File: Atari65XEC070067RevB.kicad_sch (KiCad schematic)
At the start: 340 parts, among them J1 SIO, J2 MONITOR, J5 JOY1, J6 JOY1, J7 DIN-7, J8 KEYBOARD, Q1 2N3904, Q2 2N3904, Q3 2N3904, Q4 2N3904, Q5 2N3904, Q6 2N3904, Q7 MPSA55, SW1 SW_SPDT, U1 LM358, U10 4164, U11 4164, U12 4164, U13 4164, U14 4164, U15 4164, U16 4164, U17 C014889/GTIA, U18 74LS08, U19 NE555P, U2 74LS138, U20 4050, U21 74LS74, U22 C012294/POKEY, U23 C014795 PIA/6520, U24 4051, U25 4051, U26 4164, U27 4164, U28 4164, U29 4164, U3 MMU, U30 4164, U31 4164, U32 4164, U33 4164, U34 MMMU, U35 74LS95, U4 BASIC, U5 OS ROM, U6 CO14806/SALLY, U7 C021698/ANTIC, U8 C061991/FREDDIE, U9 4164, Y2 4.33618MHz

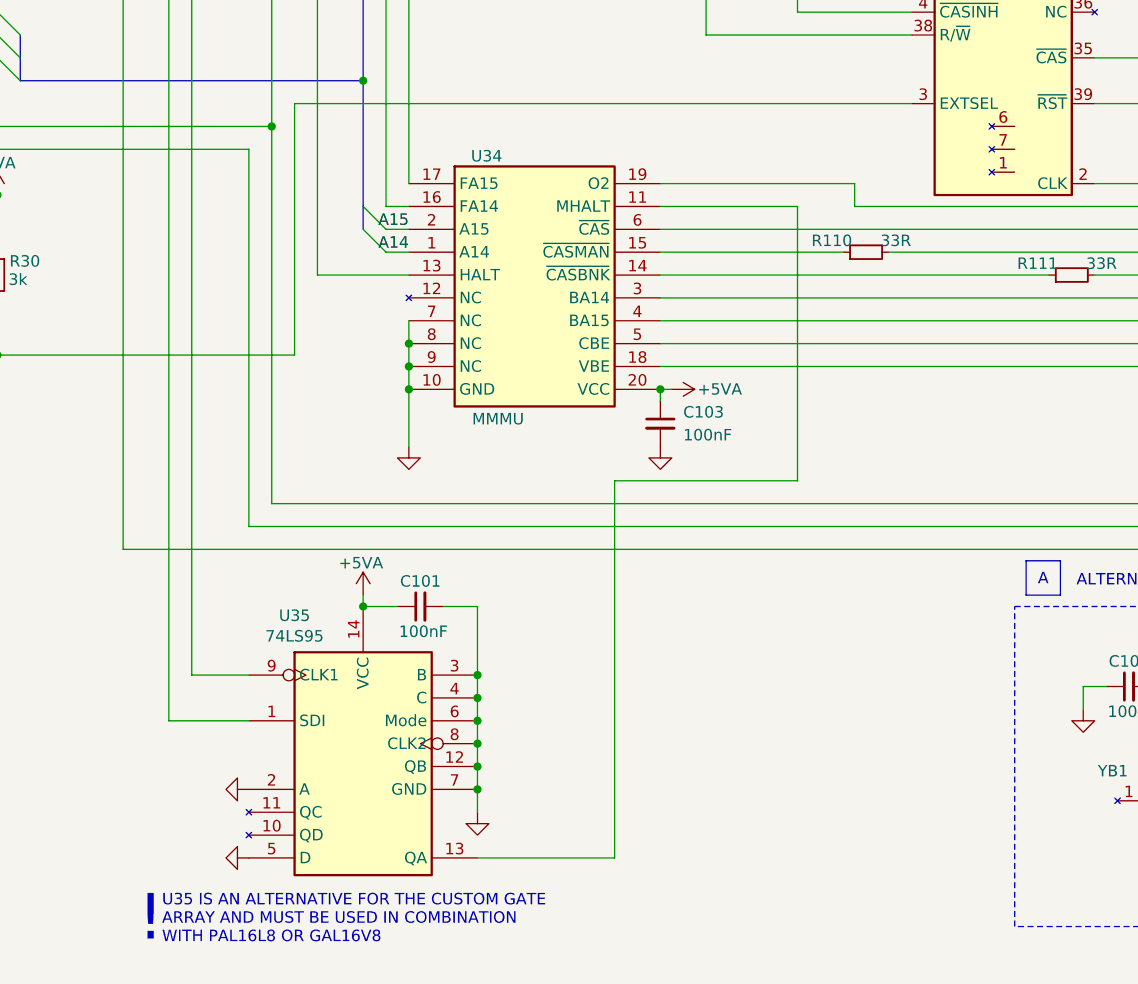
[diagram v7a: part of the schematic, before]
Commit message: update u35 and u34 schematic and routing
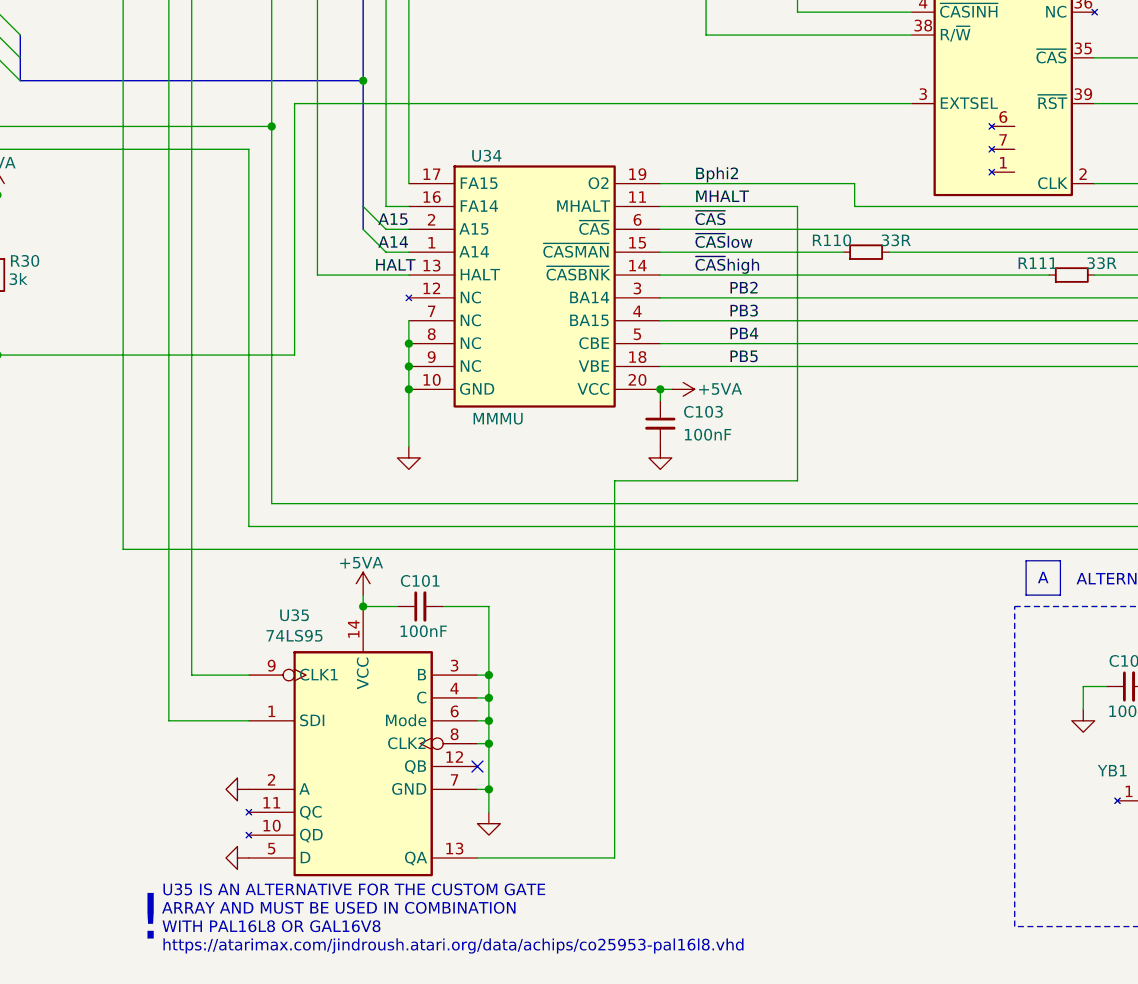
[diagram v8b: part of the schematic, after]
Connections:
- net GND: no longer U35.12 (QB)
- net PB4: now reaches R24.2, U23.14 (PB4), U34.5 (CBE)
- net MHALT: now reaches U34.11 (MHALT), U35.13 (QA)
- net ~{CAS}high: now reaches R111.1, U34.14 (~{CASBNK})
- net ~{CAS}low: now reaches R110.1, U34.15 (~{CASMAN})
- net PB5: now reaches R206.1, U23.15 (PB5), U34.18 (VBE)
- net Bphi2: now reaches R20.1, U18.1, U34.19 (O2), U6.39 (O2), U8.5 (O2)
- net PB2: now reaches R23.2, U23.12 (PB2), U34.3 (BA14)
- net PB3: now reaches R25.2, U23.13 (PB3), U34.4 (BA15)
- net ~{CAS}: now reaches U34.6 (~{CAS}), U8.35 (~{CAS})
- no-connect marks 13 -> 14
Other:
- note added: "U35 IS AN ALTERNATIVE FOR THE CUSTOM GATE ARRAY AND MUST BE USED IN COMBINATION WITH PAL16L8 OR GAL16V8 https://atarimax.com/jindroush.atari.org/data/achips/co25953-pal16l8.vhd"
- note removed: "U35 IS AN ALTERNATIVE FOR THE CUSTOM GATE ARRAY AND MUST BE USED IN COMBINATION WITH PAL16L8 OR GAL16V8"
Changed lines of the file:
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@@
 		)
 	)
-	(text "U35 IS AN ALTERNATIVE FOR THE CUSTOM GATE\nARRAY AND MUST BE USED IN COMBINATION\nWITH PAL16L8 OR GAL16V8"
+	(text "U35 IS AN ALTERNATIVE FOR THE CUSTOM GATE\nARRAY AND MUST BE USED IN COMBINATION\nWITH PAL16L8 OR GAL16V8\nhttps://atarimax.com/jindroush.atari.org/data/achips/co25953-pal16l8.vhd"
 		(exclude_from_sim no)
 		(at 55.118 400.558 0)
@@
 	)
 	(junction
-		(at 90.17 383.54)
-		(diameter 0)
-		(color 0 0 0 0)
-	)
-	(junction
 		(at 511.81 265.43)
 		(diameter 0)
@@
 	)
 	(junction
-		(at 90.17 386.08)
-		(diameter 0)
-		(color 0 0 0 0)
-	)
-	(junction
 		(at 490.22 153.67)
 		(diameter 0)
@@
 	)
 	(junction
+		(at 91.44 373.38)
+		(diameter 0)
+		(color 0 0 0 0)
+	)
+	(junction
 		(at 195.58 133.35)
 		(diameter 0)
@@
 	)
 	(junction
+		(at 91.44 378.46)
+		(diameter 0)
+		(color 0 0 0 0)
+	)
+	(junction
 		(at 384.81 336.55)
 		(diameter 0)
@@
 	)
 	(junction
+		(at 91.44 386.08)
+		(diameter 0)
+		(color 0 0 0 0)
+	)
+	(junction
 		(at 322.58 64.77)
 		(diameter 0)
@@
 	)
 	(junction
-		(at 90.17 378.46)
-		(diameter 0)
-		(color 0 0 0 0)
-	)
-	(junction
 		(at 515.62 257.81)
 		(diameter 0)
@@
 	)
 	(junction
-		(at 90.17 375.92)
-		(diameter 0)
-		(color 0 0 0 0)
-	)
-	(junction
 		(at 387.35 165.1)
 		(diameter 0)
@@
 	)
 	(junction
+		(at 91.44 375.92)
+		(diameter 0)
+		(color 0 0 0 0)
+	)
+	(junction
 		(at 278.13 317.5)
 		(diameter 0)
@@
 	)
 	(junction
+		(at 91.44 381)
+		(diameter 0)
+		(color 0 0 0 0)
+	)
+	(junction
 		(at 234.95 271.78)
 		(diameter 0)
@@
 	)
 	(junction
-		(at 90.17 381)
-		(diameter 0)
-		(color 0 0 0 0)
-	)
-	(junction
 		(at 355.6 384.81)
 		(diameter 0)
@@
 	)
 	(junction
-		(at 90.17 373.38)
-		(diameter 0)
-		(color 0 0 0 0)
-	)
-	(junction
 		(at 294.64 148.59)
 		(diameter 0)
@@
 	)
 	(no_connect
+		(at 90.17 383.54)
+	)
+	(no_connect
 		(at 284.48 201.93)
 	)
@@
 	(wire
 		(pts
-			(xy 90.17 365.76) (xy 90.17 373.38)
+			(xy 91.44 365.76) (xy 91.44 373.38)
 		)
 		(stroke
@@
 	(wire
 		(pts
-			(xy 90.17 383.54) (xy 90.17 386.08)
-		)
-		(stroke
-			(width 0)
-			(type default)
-		)
-	)
-	(wire
-		(pts
 			(xy 77.47 200.66) (xy 77.47 236.22)
 		)
@@
 	(wire
 		(pts
+			(xy 90.17 381) (xy 91.44 381)
+		)
+		(stroke
+			(width 0)
+			(type default)
+		)
+	)
+	(wire
+		(pts
 			(xy 86.36 115.57) (xy 86.36 118.11)
 		)
@@
 	(wire
 		(pts
+			(xy 91.44 381) (xy 91.44 386.08)
+		)
+		(stroke
+			(width 0)
+			(type default)
+		)
+	)
+	(wire
+		(pts
 			(xy 520.7 146.05) (xy 551.18 146.05)
 		)
@@
 	(wire
 		(pts
+			(xy 91.44 375.92) (xy 90.17 375.92)
+		)
+		(stroke
+			(width 0)
+			(type default)
+		)
+	)
+	(wire
+		(pts
 			(xy 180.34 294.64) (xy 187.96 294.64)
 		)
@@
 	(wire
 		(pts
+			(xy 91.44 378.46) (xy 90.17 378.46)
+		)
+		(stroke
+			(width 0)
+			(type default)
+		)
+	)
+	(wire
+		(pts
 			(xy 496.57 210.82) (xy 495.3 210.82)
 		)
@@
 	(wire
 		(pts
-			(xy 86.36 365.76) (xy 90.17 365.76)
+			(xy 86.36 365.76) (xy 91.44 365.76)
 		)
 		(stroke
@@
 	(wire
 		(pts
-			(xy 90.17 381) (xy 90.17 383.54)
-		)
-		(stroke
-			(width 0)
-			(type default)
-		)
-	)
-	(wire
-		(pts
 			(xy 203.2 95.25) (xy 205.74 95.25)
 		)
@@
 	(wire
 		(pts
-			(xy 90.17 375.92) (xy 90.17 378.46)
+			(xy 91.44 375.92) (xy 91.44 378.46)
 		)
 		(stroke
@@
 	(wire
 		(pts
+			(xy 91.44 373.38) (xy 90.17 373.38)
+		)
+		(stroke
+			(width 0)
+			(type default)
+		)
+	)
+	(wire
+		(pts
 			(xy 54.61 76.2) (xy 54.61 77.47)
 		)
@@
 	(wire
 		(pts
-			(xy 90.17 386.08) (xy 90.17 388.62)
+			(xy 91.44 386.08) (xy 91.44 388.62)
 		)
 		(stroke
@@
 	(wire
 		(pts
-			(xy 90.17 378.46) (xy 90.17 381)
+			(xy 91.44 378.46) (xy 91.44 381)
 		)
 		(stroke
@@
 	(wire
 		(pts
-			(xy 90.17 373.38) (xy 90.17 375.92)
+			(xy 91.44 373.38) (xy 91.44 375.92)
 		)
 		(stroke
@@
 	(wire
 		(pts
+			(xy 91.44 386.08) (xy 90.17 386.08)
+		)
+		(stroke
+			(width 0)
+			(type default)
+		)
+	)
+	(wire
+		(pts
 			(xy 419.1 181.61) (xy 419.1 243.84)
 		)
@@
 		)
 	)
+	(label "~{CAS}"
+		(at 114.3 323.85 0)
+		(effects
+			(font
+				(size 1.27 1.27)
+			)
+			(justify left bottom)
+		)
+	)
 	(label "D6"
 		(at 256.54 125.73 180)
@@
 		)
 	)
+	(label "PB2"
+		(at 118.11 331.47 0)
+		(effects
+			(font
+				(size 1.27 1.27)
+			)
+			(justify left bottom)
+		)
+	)
 	(label "D1"
 		(at 458.47 179.07 0)
@@
 		)
 	)
+	(label "~{CAS}high"
+		(at 114.3 328.93 0)
+		(effects
+			(font
+				(size 1.27 1.27)
+			)
+			(justify left bottom)
+		)
+	)
 	(label "A10"
 		(at 110.49 187.96 0)
@@
 		)
 	)
+	(label "Bphi2"
+		(at 114.3 318.77 0)
+		(effects
+			(font
+				(size 1.27 1.27)
+			)
+			(justify left bottom)
+		)
+	)
+	(label "PB3"
+		(at 118.11 334.01 0)
+		(effects
+			(font
+				(size 1.27 1.27)
+			)
+			(justify left bottom)
+		)
+	)
 	(label "D7"
 		(at 361.95 321.31 180)
@@
 		)
 	)
+	(label "PB5"
+		(at 118.11 339.09 0)
+		(effects
+			(font
+				(size 1.27 1.27)
+			)
+			(justify left bottom)
+		)
+	)
 	(label "A0"
 		(at 130.81 113.03 0)
@@
 		)
 	)
+	(label "PB4"
+		(at 118.11 336.55 0)
+		(effects
+			(font
+				(size 1.27 1.27)
+			)
+			(justify left bottom)
+		)
+	)
 	(label "A0"
 		(at 361.95 293.37 180)
@@
 		)
 	)
+	(label "MHALT"
+		(at 114.3 321.31 0)
+		(effects
+			(font
+				(size 1.27 1.27)
+			)
+			(justify left bottom)
+		)
+	)
 	(label "D6"
 		(at 154.94 187.96 0)
@@
 		)
 	)
+	(label "~{CAS}low"
+		(at 114.3 326.39 0)
+		(effects
+			(font
+				(size 1.27 1.27)
+			)
+			(justify left bottom)
+		)
+	)
 	(label "RW"
 		(at 247.65 168.91 0)
@@
 		)
 	)
+	(label "HALT"
+		(at 78.74 328.93 0)
+		(effects
+			(font
+				(size 1.27 1.27)
+			)
+			(justify left bottom)
+		)
+	)
 	(global_label "A[0..15]"
 		(shape output)
@@
 	(symbol
 		(lib_id "power:GND")
-		(at 90.17 388.62 0)
+		(at 91.44 388.62 0)
 		(mirror y)
 		(unit 1)
@@
 		(fields_autoplaced yes)
 		(property "Reference" "#PWR0120"
-			(at 90.17 394.97 0)
+			(at 91.44 394.97 0)
 			(effects
 				(font
@@
 		)
 		(property "Value" "GND"
-			(at 90.17 393.7 0)
+			(at 91.44 393.7 0)
 			(effects
 				(font
@@
 		)
 		(property "Footprint" ""
-			(at 90.17 388.62 0)
+			(at 91.44 388.62 0)
 			(effects
 				(font
@@
 		)
 		(property "Datasheet" ""
-			(at 90.17 388.62 0)
+			(at 91.44 388.62 0)
 			(effects
 				(font
@@
 		)
 		(property "Description" "Power symbol creates a global label with name \"GND\" , ground"
-			(at 90.17 388.62 0)
+			(at 91.44 388.62 0)
 			(effects
 				(font
